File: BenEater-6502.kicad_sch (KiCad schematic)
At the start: 40 parts, among them J1 Serial Header, SW11 NMI, U10 74LS00, U11 W65C22NxP, U12 HM62256BLP, U13 W65C51NxP, U14 MAX232N, U5 74LS08, U7 W65C02SxP, U8 28C256, U9 LCD-16X2, Y1 Crystal

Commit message: intermediate commit
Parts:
- removed Buttom1: Buttom, Button_Switch_THT:SW_PUSH_6mm_H5mm, symbol Switch:SW_Push
- removed C14, C15, C21: .1uf, Capacitor_THT:C_Disc_D4.3mm_W1.9mm_P5.00mm, symbol Device:C
- removed C16, C17, C18, C19: 1uf, Capacitor_THT:C_Disc_D4.3mm_W1.9mm_P5.00mm, symbol Device:C
- removed C20: 20pf, Capacitor_THT:C_Disc_D4.3mm_W1.9mm_P5.00mm, symbol Device:C
- removed D5: SB140, Diode_THT:D_DO-41_SOD81_P10.16mm_Horizontal, symbol Diode:SB140
- removed J1: Serial Header, Connector_PinHeader_2.54mm:PinHeader_1x03_P2.54mm_Vertical, symbol Connector:Conn_01x03_Pin
- removed Left1: Left, Button_Switch_THT:SW_PUSH_6mm_H5mm, symbol Switch:SW_Push
- removed Middle1: Middle, Button_Switch_THT:SW_PUSH_6mm_H5mm, symbol Switch:SW_Push
- removed R13: 1M, Resistor_THT:R_Axial_DIN0207_L6.3mm_D2.5mm_P7.62mm_Horizontal, symbol Device:R
- removed R15, R16, R17, R18, R19: 1K, Resistor_THT:R_Axial_DIN0207_L6.3mm_D2.5mm_P7.62mm_Horizontal, symbol Device:R
- removed Right1: Right, Button_Switch_THT:SW_PUSH_6mm_H5mm, symbol Switch:SW_Push
- removed Top1: Top, Button_Switch_THT:SW_PUSH_6mm_H5mm, symbol Switch:SW_Push
- removed U10: 74LS00, Package_DIP:DIP-14_W7.62mm, symbol dk_Logic-Gates-and-Inverters:SN74LS00N
- removed U13: W65C51NxP, Package_DIP:DIP-28_W15.24mm, symbol PCM_65xx-library:W65C51NxP
- removed U14: MAX232N, digikey-footprints:DIP-16_W7.62mm, symbol dk_Interface-Drivers-Receivers-Transceivers:MAX232N
- removed Y1: Crystal, Crystal:Crystal_HC18-U_Vertical, symbol Device:Crystal
- added U13: 74LS00, Package_DIP:DIP-14_W7.62mm, symbol 74xx:74LS00
- added U4 (x2): 74LS04, Package_DIP:DIP-14_W7.62mm, symbol 8bit-computer-rescue:74LS04-8bit-computer-rescue
- added U6: 74LS32, Package_DIP:DIP-14_W7.62mm, symbol 8bit-computer-rescue:74LS32-8bit-computer-rescue
- renumbered C10 to C15, C11 to C16, C12 to C17, C13 to C18, D7 to D5, R20 to R15, R12 to R16, SW11 to SW5, U12 to U10, U9 to U12, U7 to U8, U8 to U9
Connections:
- net A14: now also U13.10
- net A15: now also U13.1, U13.2
- net A4: now also U6.1
- net CLK: now also U13.5
- net Earth: no longer RV2.3
- net GND: now also U4.7 (GND), U4.7 (GND), U6.7 (GND)
- net HLT: no longer U11.17 (PB7)
- net R/W: now also U4.1
- net VCC: now also U4.14 (VCC), U4.14 (VCC), U6.14 (VCC)
- net RTSVia: now reaches U11.2 (PA0)
- net at U11.23 (~{CS2}): now also U4.1, U6.3
- net at U10.20 (~{CS}): now also U13.6
- net at U9.20 (~{CS}): now also U13.3, U13.4, U13.9
- net at U9.22 (~{OE}): now also U4.2
- new net CS2: U13.8, U6.2
- new net CS2Via2: U4.2
- no-connect marks 15 -> 22
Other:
- added sheet Serial (serial.kicad_sch)
- sheet Expansion & Diag ports: added CS2Via2; removed none

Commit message: interm commit
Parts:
- removed U6: 74LS32, Package_DIP:DIP-14_W7.62mm, symbol 8bit-computer-rescue:74LS32-8bit-computer-rescue
- added C27: .1uf, Capacitor_THT:C_Disc_D4.3mm_W1.9mm_P5.00mm, symbol Device:C
- added J14: Conn_01x10, Connector_PinSocket_1.27mm:PinSocket_1x10_P1.27mm_Vertical, symbol Connector_Generic:Conn_01x10
- added R25: 1K, Resistor_THT:R_Axial_DIN0207_L6.3mm_D2.5mm_P7.62mm_Horizontal, symbol Device:R
- added unit 4 of U13
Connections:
- net +5V: now also C27.1, J14.1 (Pin_1), R25.1
- net A4: now also U4.1
- net BE: now also R25.2
- net CS2: now also U11.23 (~{CS2}), U13.13
- net Earth: now also C27.2, J14.10 (Pin_10)
- net RTSVia: now also J14.2 (Pin_2)
- net at U11.13 (PB3), U12.14 (DB7): now also U11.14 (PB4), U12.4 (RS)
- net at U11.3 (PA1): now also J14.3 (Pin_3)
- net at U11.4 (PA2): now also J14.4 (Pin_4)
- net at U11.5 (PA3): now also J14.5 (Pin_5)
- net at U11.6 (PA4): now also J14.6 (Pin_6)
- net at U11.7 (PA5): now also J14.7 (Pin_7)
- net at U11.8 (PA6): now also J14.8 (Pin_8)
- net at U11.9 (PA7): now also J14.9 (Pin_9)
- net at U13.6: now also U13.12; no longer U10.20 (~{CS})
- new net: U10.20 (~{CS}), U13.11
- no-connect marks 22 -> 15
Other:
- moved on the sheet: RV2, U12, U13C, U4A

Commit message: An other interm relase
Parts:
- removed U13: 74LS00, Package_DIP:DIP-14_W7.62mm, symbol 74xx:74LS00
- removed U4: 74LS04, Package_DIP:DIP-14_W7.62mm, symbol 8bit-computer-rescue:74LS04-8bit-computer-rescue
- removed U5: 74LS08, Package_DIP:DIP-14_W7.62mm, symbol 8bit-computer-rescue:74LS08-8bit-computer-rescue
- J14: footprint Connector_PinSocket_1.27mm:PinSocket_1x10_P1.27mm_Vertical -> Connector_PinSocket_2.54mm:PinSocket_1x10_P2.54mm_Vertical
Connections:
- net at U11.13 (PB3), U12.14 (DB7): no longer U11.14 (PB4), U12.4 (RS)
- net RAMOE: now reaches U10.22 (~{OE})
- net ROMCS: now reaches U9.20 (~{CS})
- net RAMCS: now reaches U10.20 (~{CS})
- new net: U11.14 (PB4), U12.4 (RS)
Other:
- added sheet Control Logic (control.kicad_sch)

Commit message: Fix Oops...
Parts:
- C15, C16, C17, C18, C27: value .1uf -> 0.1uf
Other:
- moved on the sheet: U4A
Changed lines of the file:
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@@
 	)
 	(junction
-		(at 234.315 32.385)
+		(at 91.186 119.38)
 		(diameter 0)
 		(color 0 0 0 0)
 	)
 	(junction
-		(at 68.58 189.23)
+		(at 234.315 32.385)
 		(diameter 0)
 		(color 0 0 0 0)
 	)
 	(junction
-		(at 100.33 119.38)
+		(at 68.58 189.23)
 		(diameter 0)
 		(color 0 0 0 0)
@@
 	(wire
 		(pts
-			(xy 50.8 119.38) (xy 100.33 119.38)
+			(xy 50.8 119.38) (xy 91.186 119.38)
 		)
 		(stroke
@@
 	(wire
 		(pts
-			(xy 100.33 119.38) (xy 187.96 119.38)
-		)
-		(stroke
-			(width 0)
-			(type default)
-		)
-	)
-	(wire
-		(pts
 			(xy -16.51 85.09) (xy -16.51 87.63)
 		)
@@
 		)
 	)
-	(wire
-		(pts
-			(xy 106.68 101.6) (xy 124.46 101.6)
-		)
-		(stroke
-			(width 0)
-			(type default)
-		)
-	)
 	(bus
 		(pts
@@
 	(wire
 		(pts
+			(xy 91.186 119.38) (xy 91.186 125.984)
+		)
+		(stroke
+			(width 0)
+			(type default)
+		)
+	)
+	(wire
+		(pts
 			(xy 85.09 62.23) (xy 86.36 62.23)
 		)
@@
 	(wire
 		(pts
-			(xy 100.33 78.74) (xy 100.33 119.38)
-		)
-		(stroke
-			(width 0)
-			(type default)
-		)
-	)
-	(wire
-		(pts
 			(xy 161.29 86.36) (xy 162.56 86.36)
 		)
@@
 	(wire
 		(pts
+			(xy 91.186 119.38) (xy 187.96 119.38)
+		)
+		(stroke
+			(width 0)
+			(type default)
+		)
+	)
+	(wire
+		(pts
 			(xy 226.06 81.28) (xy 229.87 81.28)
 		)
@@
 	(wire
 		(pts
+			(xy 114.046 101.6) (xy 114.046 125.984)
+		)
+		(stroke
+			(width 0)
+			(type default)
+		)
+	)
+	(wire
+		(pts
 			(xy -1.27 73.66) (xy 2.54 73.66)
 		)
@@
 	(wire
 		(pts
-			(xy 106.68 78.74) (xy 100.33 78.74)
-		)
-		(stroke
-			(width 0)
-			(type default)
-		)
-	)
-	(wire
-		(pts
 			(xy -39.37 141.986) (xy -31.75 141.986)
 		)
@@
 	(wire
 		(pts
+			(xy 114.046 101.6) (xy 124.46 101.6)
+		)
+		(stroke
+			(width 0)
+			(type default)
+		)
+	)
+	(wire
+		(pts
 			(xy 235.585 86.36) (xy 226.06 86.36)
 		)
@@
 		)
 	)
-	(wire
+	(bus
 		(pts
-			(xy 124.46 104.14) (xy 115.57 104.14)
+			(xy 201.93 101.6) (xy 201.93 104.14)
 		)
 		(stroke
@@
 		)
 	)
-	(bus
+	(wire
 		(pts
-			(xy 201.93 101.6) (xy 201.93 104.14)
+			(xy 144.78 58.42) (xy 146.05 58.42)
 		)
 		(stroke
@@
 	(wire
 		(pts
-			(xy 144.78 58.42) (xy 146.05 58.42)
+			(xy 233.68 93.98) (xy 226.06 93.98)
 		)
 		(stroke
@@
 	(wire
 		(pts
-			(xy 233.68 93.98) (xy 226.06 93.98)
+			(xy 36.83 72.39) (xy 36.83 74.93)
 		)
 		(stroke
@@
 	(wire
 		(pts
-			(xy 36.83 72.39) (xy 36.83 74.93)
+			(xy 119.634 104.14) (xy 124.46 104.14)
 		)
 		(stroke
@@
 		)
 	)
+	(label "A13"
+		(at 3.048 143.51 0)
+		(fields_autoplaced yes)
+		(effects
+			(font
+				(size 0.5 0.5)
+			)
+			(justify left bottom)
+		)
+	)
 	(label "A10"
 		(at 86.36 72.39 0)
@@
 		)
 	)
+	(label "A15"
+		(at 3.048 140.462 0)
+		(fields_autoplaced yes)
+		(effects
+			(font
+				(size 0.5 0.5)
+			)
+			(justify left bottom)
+		)
+	)
 	(label "A7"
 		(at 2.54 73.66 0)
@@
 	)
 	(label "ROMCS"
-		(at 115.57 104.14 180)
+		(at 119.888 104.14 180)
 		(fields_autoplaced yes)
 		(effects
@@
 		)
 	)
+	(label "CLK"
+		(at 3.048 151.384 0)
+		(fields_autoplaced yes)
+		(effects
+			(font
+				(size 0.5 0.5)
+			)
+			(justify left bottom)
+		)
+	)
 	(label "A4"
 		(at 123.19 68.58 180)
@@
 		)
 	)
+	(label "A14"
+		(at 3.048 141.986 0)
+		(fields_autoplaced yes)
+		(effects
+			(font
+				(size 0.5 0.5)
+			)
+			(justify left bottom)
+		)
+	)
 	(label "D0"
 		(at 86.36 90.17 0)
@@
 		)
 	)
+	(label "A12"
+		(at 3.048 145.034 0)
+		(fields_autoplaced yes)
+		(effects
+			(font
+				(size 0.5 0.5)
+			)
+			(justify left bottom)
+		)
+	)
 	(label "Reset"
 		(at 2.54 49.53 0)
@@
 		)
 	)
+	(label "A4"
+		(at 3.048 146.558 0)
+		(fields_autoplaced yes)
+		(effects
+			(font
+				(size 0.5 0.5)
+			)
+			(justify left bottom)
+		)
+	)
 	(label "A12"
 		(at 123.19 88.9 180)
@@
 	(symbol
 		(lib_id "8bit-computer-rescue:74LS04-8bit-computer-rescue")
-		(at 106.68 90.17 270)
+		(at 102.616 125.984 0)
+		(mirror x)
 		(unit 1)
 		(exclude_from_sim no)
@@
 		(dnp no)
 		(property "Reference" "U4"
-			(at 109.601 95.123 0)
+			(at 107.569 128.905 0)
 			(effects
 				(font
@@
 		)
 		(property "Value" "74LS04"
-			(at 103.505 94.996 0)
+			(at 107.442 122.809 0)
 			(effects
 				(font
@@
 		)
 		(property "Footprint" "Package_DIP:DIP-14_W7.62mm"
-			(at 106.68 90.17 0)
+			(at 102.616 125.984 0)
 			(effects
 				(font
@@
 		)
 		(property "Datasheet" ""
-			(at 106.68 90.17 0)
+			(at 102.616 125.984 0)
 			(effects
 				(font
@@
 		)
 		(property "Description" ""
-			(at 106.68 90.17 0)
+			(at 102.616 125.984 0)
 			(effects
 				(font
@@
 			)
 		)
-		(property "Value" ".1uf"
+		(property "Value" "0.1uf"
 			(at 46.355 194.945 0)
 			(effects
@@
 			)
 		)
-		(property "Value" ".1uf"
+		(property "Value" "0.1uf"
 			(at 67.945 194.945 0)
 			(effects
@@
 			)
 		)
-		(property "Value" ".1uf"
+		(property "Value" "0.1uf"
 			(at 77.47 194.945 0)
 			(effects
@@
 			)
 		)
-		(property "Value" ".1uf"
+		(property "Value" "0.1uf"
 			(at 56.515 194.945 0)
 			(effects
@@
 			)
 		)
-		(property "Value" ".1uf"
+		(property "Value" "0.1uf"
 			(at 36.195 194.945 0)
 			(effects

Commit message: Closer yet
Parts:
- removed D5: SB140, Diode_THT:D_DO-41_SOD81_P10.16mm_Horizontal, symbol Diode:SB140
- removed U4: 74LS04, Package_DIP:DIP-14_W7.62mm, symbol 8bit-computer-rescue:74LS04-8bit-computer-rescue
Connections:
- net Earth: now also U9.22 (~{OE})
- net IRQ: now also U11.21 (~{IRQ})
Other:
- sheet Control Logic ports: added none; removed A12, A13, A4, CS2Via2
- sheet Expansion & Diag ports: added CS2; removed CS2Via2

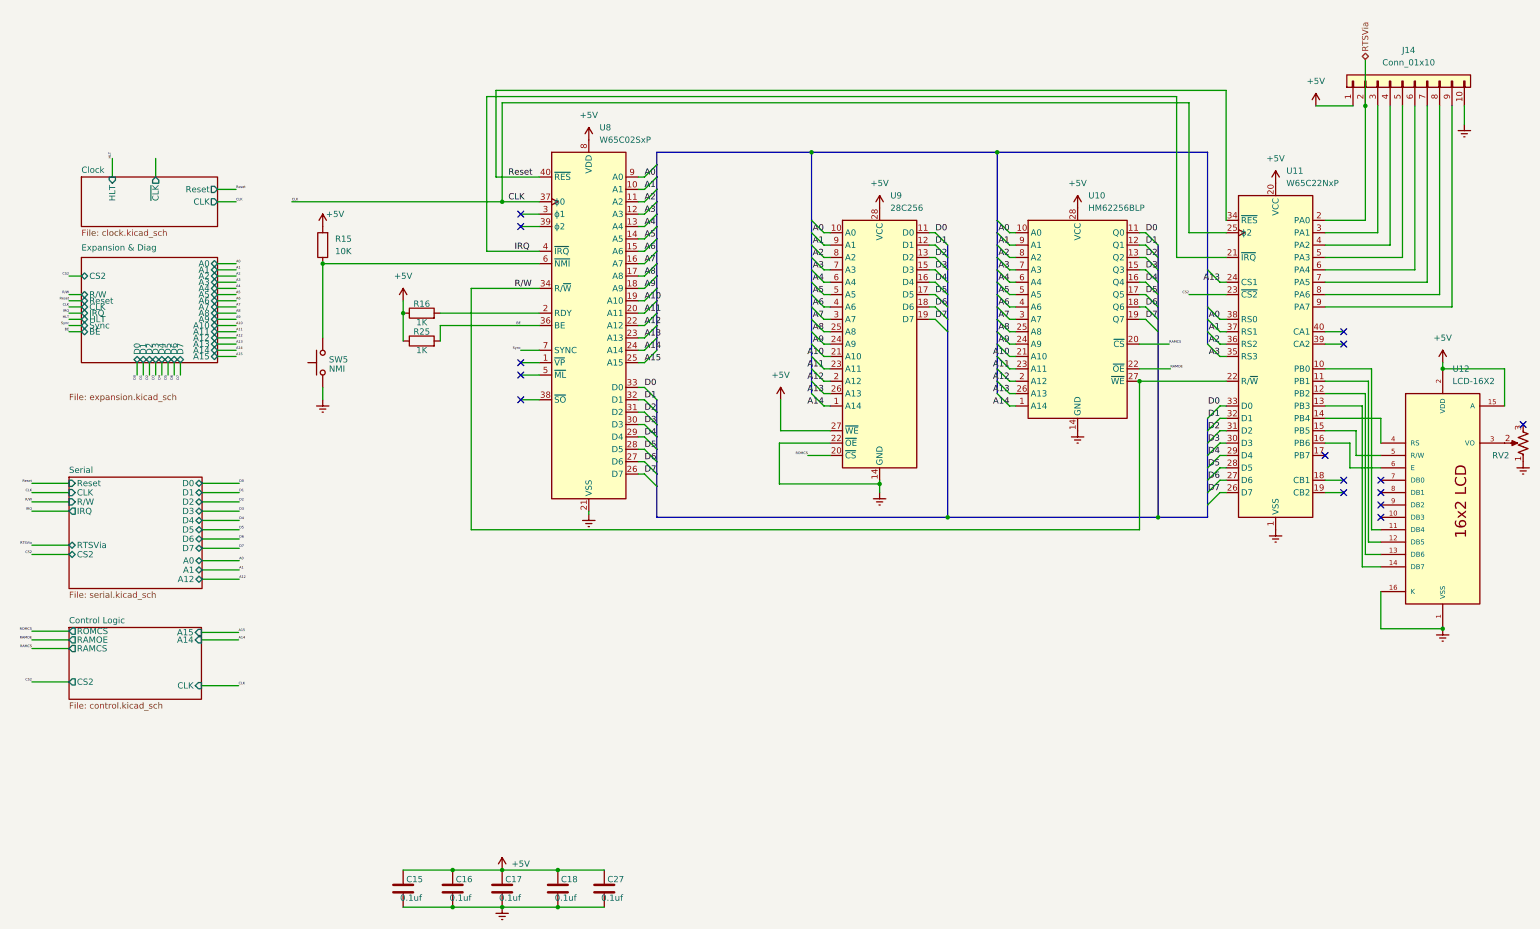
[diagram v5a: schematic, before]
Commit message: Fixed the addressing Still not fixed
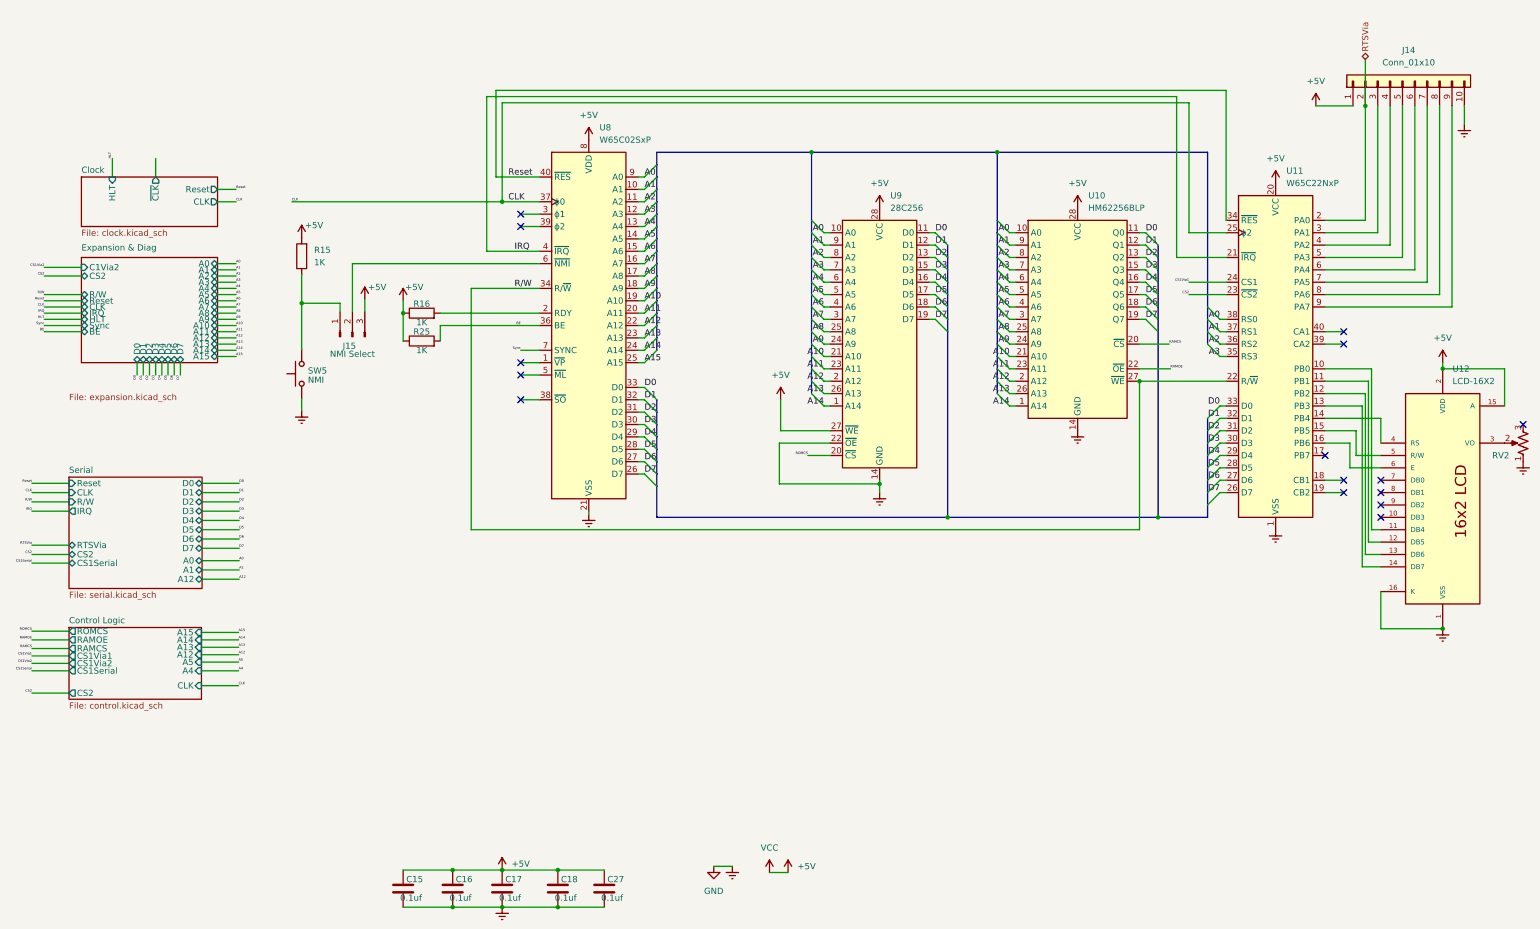
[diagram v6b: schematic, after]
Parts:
- added J15: NMI Select, Connector_PinSocket_2.54mm:PinSocket_1x03_P2.54mm_Vertical, symbol Connector:Conn_01x03_Pin
- R15: value 10K -> 1K
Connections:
- net +5V: now also J15.3 (Pin_3)
- net A13: no longer U11.24 (CS1)
- net at R15.1, SW5.2: now also J15.1 (Pin_1); no longer U8.6 (~{NMI})
- new net: J15.2 (Pin_2), U8.6 (~{NMI})
- new net CS1Via1: U11.24 (CS1)
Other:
- sheet Control Logic ports: added A12, A13, A4, A5, CS1Serial, CS1Via1, CS1Via2; removed none
- sheet Expansion & Diag ports: added C1Via2; removed none
- sheet Serial ports: added CS1Serial; removed none
- moved on the sheet: R15, SW5

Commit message: It works
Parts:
- added D5: SB140, Diode_THT:D_DO-41_SOD81_P10.16mm_Horizontal, symbol Diode:SB140
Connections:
- net IRQ: now also D5.2 (A); no longer U11.21 (~{IRQ})
- new net: D5.1 (K), U11.21 (~{IRQ})
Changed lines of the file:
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@@
 	(wire
 		(pts
+			(xy 195.58 30.48) (xy 195.58 44.45)
+		)
+		(stroke
+			(width 0)
+			(type default)
+		)
+	)
+	(wire
+		(pts
 			(xy -1.27 81.28) (xy 2.54 81.28)
 		)
@@
 	(wire
 		(pts
-			(xy 195.58 30.48) (xy 195.58 63.5)
-		)
-		(stroke
-			(width 0)
-			(type default)
-		)
-	)
-	(wire
-		(pts
 			(xy 194.056 81.28) (xy 187.96 81.28)
 		)
@@
 	(wire
 		(pts
+			(xy 195.58 52.07) (xy 195.58 63.5)
+		)
+		(stroke
+			(width 0)
+			(type default)
+		)
+	)
+	(wire
+		(pts
 			(xy 237.49 96.52) (xy 237.49 101.6)
 		)
@@
 					(unit 1)
 				)
+			)
+		)
+	)
+	(symbol
+		(lib_id "Diode:SB140")
+		(at 195.58 48.26 90)
+		(unit 1)
+		(exclude_from_sim no)
+		(in_bom yes)
+		(on_board yes)
+		(dnp no)
+		(fields_autoplaced yes)
+		(property "Reference" "D5"
+			(at 198.12 47.3074 90)
+			(effects
+				(font
+					(size 1.27 1.27)
+				)
+				(justify right)
+			)
+		)
+		(property "Value" "SB140"
+			(at 198.12 49.8474 90)
+			(effects
+				(font
+					(size 1.27 1.27)
+				)
+				(justify right)
+			)
+		)
+		(property "Footprint" "Diode_THT:D_DO-41_SOD81_P10.16mm_Horizontal"
+			(at 200.025 48.26 0)
+			(effects
+				(font
+					(size 1.27 1.27)
+				)
+				(hide yes)
+			)
+		)
+		(property "Datasheet" "http://www.diodes.com/_files/datasheets/ds23022.pdf"
+			(at 195.58 48.26 0)
+			(effects
+				(font
+					(size 1.27 1.27)
+				)
+				(hide yes)
+			)
+		)
+		(property "Description" "40V 1A Schottky Barrier Rectifier Diode, DO-41"
+			(at 195.58 48.26 0)
+			(effects
+				(font
+					(size 1.27 1.27)
+				)
+				(hide yes)
+			)
+		)
+		(pin "2"
+		)
+		(pin "1"
+		)
+		(instances
+			(project ""
+				(path "/64020bd5-bae0-49a1-9410-23726bcfaf48"
+					(reference "D5")
+					(unit 1)
+				)
